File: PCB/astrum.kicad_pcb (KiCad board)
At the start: 4 copper layers, 45.5 x 69.8 mm, 60 parts, among them J1 USB_C_Receptacle_USB2.0_16P, J10 Conn_01x05_Pin, J11 Screw_Terminal_01x02, J2 Micro_SD_Card, J3 Screw_Terminal_01x02, J5 Conn_01x04_MountingPin, J6 Conn_01x04_MountingPin, J7 Conn_01x10_Pin, J8 Conn_01x10_Pin, J9 Conn_01x05_Pin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

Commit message: update production files
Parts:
- removed the G*** at (152.8, 124.0)
- removed the G*** at (146.8, 129.1)
- removed the G*** at (144.0, 129.1)
- removed the G*** at (153.0, 108.8)
- removed the G*** at (159.5, 129.1)
- removed the G*** at (142.8, 108.8)
- removed the G*** at (138.0, 124.0)
- removed the G*** at (131.2, 129.1)
- added C21: 100nF, A_HDJ_Library:C_0603_1608Metric, F.Cu at (162.3, 123.9)
- added C22: 100nF, A_HDJ_Library:C_0402_1005Metric, F.Cu at (149.4, 99.8)
- added G***: LOGO, LOGO, F.Cu at (146.3, 111.1)
- added G***: LOGO, LOGO, F.Cu at (156.5, 111.1)
- added G***: LOGO, LOGO, F.Cu at (134.8, 131.4)
- added G***: LOGO, LOGO, F.Cu at (147.5, 131.4)
- added G***: LOGO, LOGO, F.Cu at (163.0, 131.4)
- added G***: LOGO, LOGO, F.Cu at (156.3, 126.4)
- added G***: LOGO, LOGO, F.Cu at (150.3, 131.4)
- added G***: LOGO, LOGO, F.Cu at (141.5, 126.4)
- added R6: 4.7k, Resistor_SMD:R_0603_1608Metric, F.Cu at (152.9, 88.5)
- added R8: 10k, Resistor_SMD:R_0603_1608Metric, F.Cu at (135.3, 124.5)
- added SW1: TS-1088-AR02016, easyeda2kicad:SW-SMD_L3.9-W3.0-P4.45, F.Cu at (161.5, 119.8)
- added SW2: TS-1088-AR02016, easyeda2kicad:SW-SMD_L3.9-W3.0-P4.45, F.Cu at (136.1, 119.8)
- C18: value C_Polarized_Small -> 22uF
- C2: footprint A_HDJ_Library:C_0603_1608Metric -> lpddr4-testbed-footprints:C_0402_1005Metric
- moved C2 15.0 mm to (153.6, 92.1), turned to 0 degrees
- moved C12 4.24 mm to (136.3, 91.6)
- moved C18 4.24 mm to (148.9, 116.7)
- moved D3 4.24 mm to (137.1, 82.1)
- moved J3 4.24 mm to (138.8, 131.4)
- moved J5 4.24 mm to (132.7, 111.7)
- moved R3 4.24 mm to (145.5, 121.8)
- moved U4 4.24 mm to (158.4, 94.8)
- moved U9 4.24 mm to (156.0, 119.6)
- moved J2 4.24 mm to (154.7, 79.0)
- moved J8 4.24 mm to (131.5, 80.9)
- moved R2 4.24 mm to (133.4, 76.4)
- moved C1 4.24 mm to (142.5, 96.4)
- moved C10 4.24 mm to (137.7, 89.5)
- moved C11 4.24 mm to (158.4, 100.3)
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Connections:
- U1 pad 44: unconnected-(U1-BOOT0-Pad44) -> BOOT0
- U1 pad 7: unconnected-(U1-NRST-Pad7) -> NRST
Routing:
- net BOOT0: track 0.00 -> 38.7 mm, vias 0 -> 2
- net NRST: track 0.00 -> 37.5 mm, vias 0 -> 3
- net VDD: track 89.9 -> 92.9 mm, vias 16 -> 18
- net unconnected-(U1-BOOT0-Pad44): track 0.66 -> 0.00 mm, vias 1 -> 0
- net GND: vias 37 -> 35
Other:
- outline, holes or cut-outs redrawn

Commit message: make the board cheaper?
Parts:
- removed C14: 100nF, A_HDJ_Library:C_0603_1608Metric
- removed the G*** at (146.3, 111.1)
- removed the G*** at (156.5, 111.1)
- removed the G*** at (134.8, 131.4)
- removed the G*** at (147.5, 131.4)
- removed the G*** at (163.0, 131.4)
- removed the G*** at (156.3, 126.4)
- removed the G*** at (150.3, 131.4)
- removed the G*** at (141.5, 126.4)
- removed U5: ICM-20948, Sensor_Motion:InvenSense_QFN-24_3x3mm_P0.4mm
- removed Y1: 25 mHz, Crystal:Crystal_SMD_Abracon_ABM3-2Pin_5.0x3.2mm
- added G***: LOGO, LOGO, F.Cu at (135.7, 132.5)
- added G***: LOGO, LOGO, F.Cu at (157.2, 127.5)
- added G***: LOGO, LOGO, F.Cu at (151.2, 132.5)
- added G***: LOGO, LOGO, F.Cu at (157.5, 111.7)
- added G***: LOGO, LOGO, F.Cu at (142.5, 127.5)
- added G***: LOGO, LOGO, F.Cu at (147.3, 111.7)
- added G***: LOGO, LOGO, F.Cu at (164.0, 132.5)
- added G***: LOGO, LOGO, F.Cu at (148.5, 132.5)
- added R10: 10k, Resistor_SMD:R_0603_1608Metric, F.Cu at (137.3, 108.0)
- added R9: 10k, Resistor_SMD:R_0603_1608Metric, F.Cu at (140.3, 108.0)
- added U11: LD39015M18R, Package_TO_SOT_SMD:SOT-23-5, F.Cu at (137.9, 95.2)
- added Y2: 25mHz, Crystal:Crystal_SMD_3225-4Pin_3.2x2.5mm, F.Cu at (148.7, 104.7)
- C18: footprint Capacitor_SMD:CP_Elec_3x5.3 -> Capacitor_SMD:CP_Elec_4x5.4
- C20: value C_Polarized_Small -> 22uF; footprint Capacitor_SMD:CP_Elec_3x5.3 -> Capacitor_SMD:CP_Elec_4x5.4
- C7, C8: value 5.6pF -> 12pF
- U6: value MIC5317-1.8xM5 -> LSM6DSR; footprint Package_TO_SOT_SMD:SOT-23-5 -> LSM6DSR:LGA_M6DSR_STM
- moved U6 11.7 mm to (139.3, 105.5), turned to 180 degrees
- moved C16 3.52 mm to (139.0, 103.1), turned to 180 degrees
- moved C7 2.34 mm to (145.7, 104.8)
- moved C15 2.12 mm to (136.6, 105.6), turned to -90 degrees
- moved C20 1.85 mm to (149.8, 124.3)
- moved C21 1.47 mm to (163.2, 125.0)
- moved H1 1.47 mm to (130.0, 73.7)
- moved H2 1.47 mm to (169.5, 73.5)
- moved J7 1.47 mm to (167.0, 82.0)
- moved U1 1.47 mm to (149.4, 95.8)
- moved C11 1.47 mm to (159.4, 101.4)
- moved C13 1.47 mm to (140.7, 95.2)
- moved C2 1.47 mm to (154.6, 93.2)
- moved C3 1.47 mm to (145.8, 88.9)
- moved C5 1.47 mm to (145.8, 90.5)
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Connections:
- C15 pad 1: +1V8 -> VDD
- C16 pad 1: +1V8 -> VDD
- J7 pad 10: unconnected-(J7-Pin_10-Pad10) -> GND
- J7 pad 9: unconnected-(J7-Pin_9-Pad9) -> GND
- J8 pad 10: GPIO8 -> unconnected-(J8-Pin_10-Pad10)
- U6 pad 1: VDD -> unconnected-(U6-SDO/SA0-Pad1)
- U6 pad 2: GND -> unconnected-(U6-SDX-Pad2)
- U6 pad 3: VDD -> unconnected-(U6-SCX-Pad3)
- U6 pad 4: unconnected-(U6-NC-Pad4) -> GPIO8
- U6 pad 5: +1V8 -> VDD
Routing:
- net IMU_SDA: track 66.8 -> 83.2 mm, vias 4 -> 6
- net IMU_SCL: track 68.3 -> 83.9 mm, vias 4 -> 5
- net +1V8: track 97.9 -> 82.9 mm, vias 12 -> 9
- net IMU_INT: track 22.9 -> 36.2 mm, vias 2 -> 4
- net VDD: track 92.9 -> 102.0 mm, vias 18 -> 21
- net GPIO8: track 19.7 -> 12.9 mm, vias 1 -> 2
- net /SCL_1V8: track 10.5 -> 3.76 mm
- net /SDA_1V8: track 6.44 -> 1.58 mm
- net /INT_1V8: track 32.4 -> 29.6 mm, vias 2 -> 1
- net unconnected-(U5-SDO/AD0-Pad9): track 2.27 -> 0.00 mm, vias 1 -> 0
- net Net-(U5-REGOUT): track 2.22 -> 0.00 mm
- net Net-(U1-PH1): track 8.97 -> 6.77 mm
- net /FSYNC_1V8: track 2.72 -> 1.60 mm, vias 1 -> 0
- net GND: vias 35 -> 38
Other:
- board size 45.5 x 69.8 mm -> 45.5 x 69.7 mm

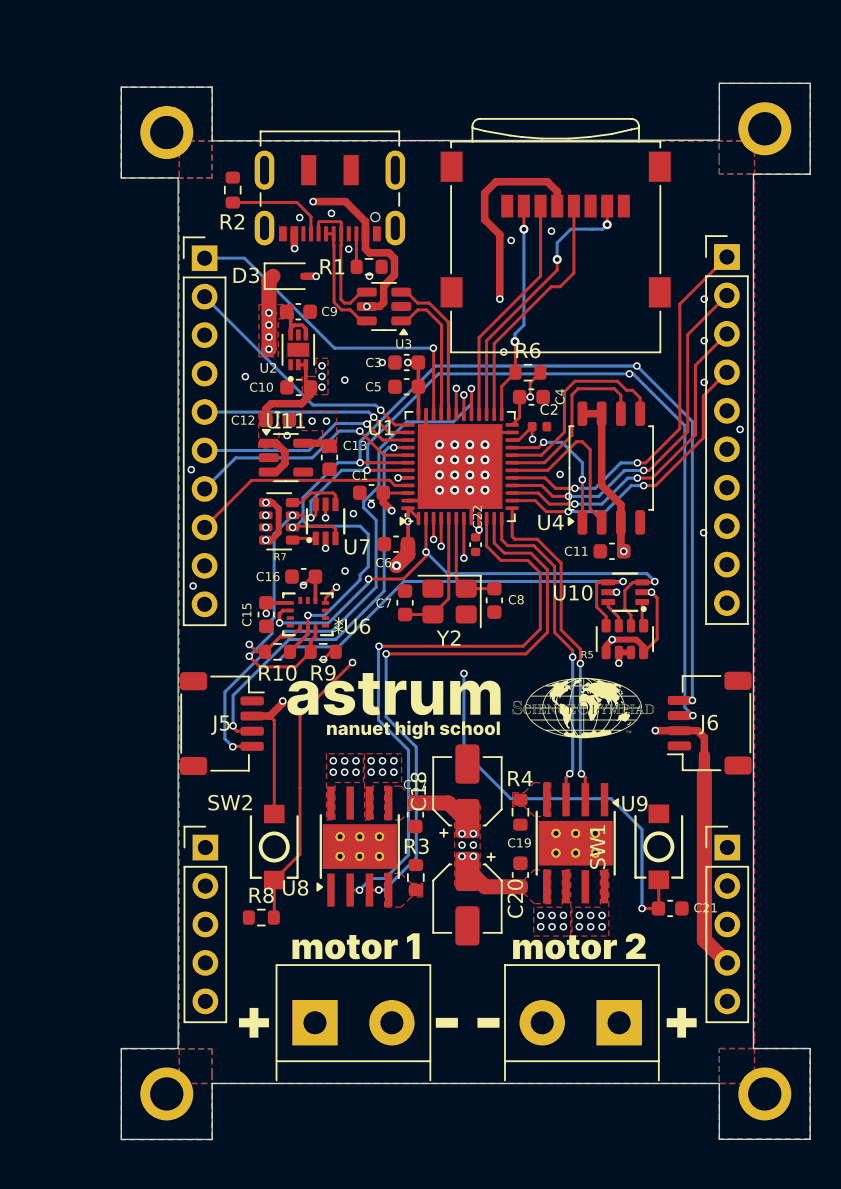
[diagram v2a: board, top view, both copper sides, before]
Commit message: fix oscillator
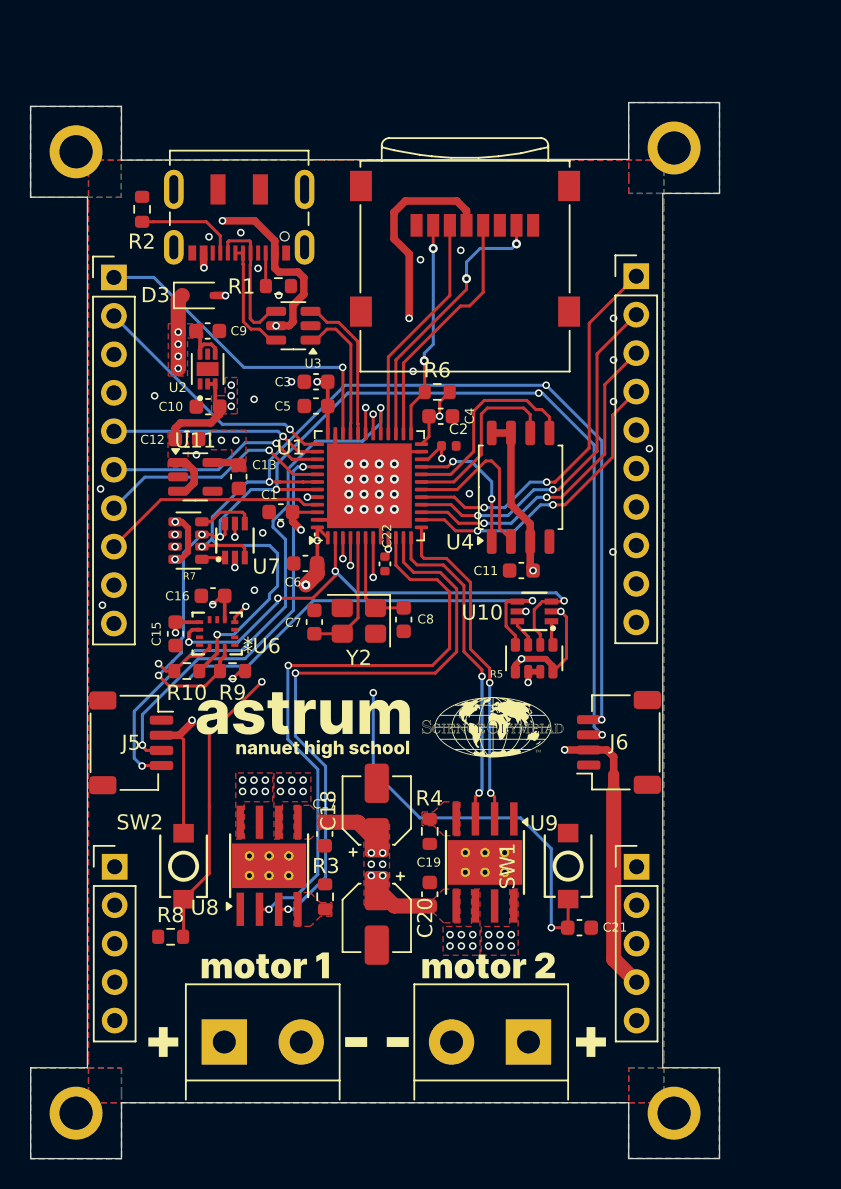
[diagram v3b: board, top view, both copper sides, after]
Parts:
- removed the G*** at (135.7, 132.5)
- removed the G*** at (157.2, 127.5)
- removed the G*** at (151.2, 132.5)
- removed the G*** at (157.5, 111.7)
- removed the G*** at (142.5, 127.5)
- removed the G*** at (147.3, 111.7)
- removed the G*** at (164.0, 132.5)
- removed the G*** at (148.5, 132.5)
- added G***: LOGO, LOGO, F.Cu at (141.3, 113.0)
- added G***: LOGO, LOGO, F.Cu at (151.5, 113.0)
- added G***: LOGO, LOGO, F.Cu at (129.8, 133.8)
- added G***: LOGO, LOGO, F.Cu at (136.5, 128.8)
- added G***: LOGO, LOGO, F.Cu at (145.2, 133.8)
- added G***: LOGO, LOGO, F.Cu at (142.5, 133.8)
- added G***: LOGO, LOGO, F.Cu at (151.2, 128.8)
- added G***: LOGO, LOGO, F.Cu at (158.0, 133.8)
- moved C13 6.12 mm to (134.7, 96.5)
- moved C15 6.12 mm to (130.6, 106.8)
- moved C2 6.12 mm to (148.6, 94.4)
- moved C5 6.12 mm to (139.8, 91.8)
- moved C8 6.12 mm to (145.6, 105.9)
- moved H3 6.12 mm to (163.5, 138.5)
- moved H4 6.12 mm to (124.0, 138.5)
- moved J11 6.12 mm to (153.9, 133.8)
- moved J3 6.12 mm to (133.8, 133.8)
- moved R5 6.12 mm to (154.3, 108.5)
- moved SW1 6.12 mm to (156.5, 122.2)
- moved U2 6.12 mm to (132.7, 89.4)
- moved U3 6.12 mm to (138.3, 86.5)
- moved C11 6.12 mm to (153.4, 102.7)
- moved C12 6.12 mm to (131.3, 94.0)
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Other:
- board size 45.5 x 69.7 mm -> 45.5 x 69.8 mm

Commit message: fix some dum vcap thingies
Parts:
- U2: footprint LDL212PV33R:SON50P200X200X80-7N -> LDL212PV33R:DFN_V33R_STM
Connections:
- net GPIO8 renamed IMU_INT1
- C1 pad 1: VDD -> Net-(C1-Pad1)
- C2 pad 1: VDD -> Net-(C1-Pad1)
- U1 pad 22: VDD -> Net-(C1-Pad1)
- U1 pad 46: VDD -> Net-(C1-Pad1)
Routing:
- net Net-(C1-Pad1): track 0.00 -> 18.7 mm, vias 0 -> 2
- net VDD: track 102.0 -> 96.3 mm, vias 21 -> 19

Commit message: update stuff again
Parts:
- removed the G*** at (141.3, 113.0)
- removed the G*** at (151.5, 113.0)
- removed the G*** at (129.8, 133.8)
- removed the G*** at (136.5, 128.8)
- removed the G*** at (145.2, 133.8)
- removed the G*** at (142.5, 133.8)
- removed the G*** at (151.2, 128.8)
- removed the G*** at (158.0, 133.8)
- added ?: , clipboard:975089c0-34e4-4fa3-ba18-6809d370517a, B.Cu at (162.0, 125.8)
- added ?: , clipboard:975089c0-34e4-4fa3-ba18-6809d370517a, B.Cu at (146.9, 125.8)
- added G***: LOGO, LOGO, F.Cu at (157.0, 108.8)
- added G***: LOGO, LOGO, B.Cu at (135.2, 129.6)
- added G***: LOGO, LOGO, B.Cu at (150.7, 129.6)
- added G***: LOGO, LOGO, B.Cu at (142.0, 124.5)
- added G***: LOGO, LOGO, B.Cu at (156.7, 124.5)
- added G***: LOGO, LOGO, B.Cu at (148.0, 129.6)
- added G***: LOGO, LOGO, B.Cu at (154.2, 93.5)
- added G***: LOGO, LOGO, B.Cu at (163.5, 129.6)
- added G***: LOGO, LOGO, F.Cu at (146.8, 108.8)
- added G***: LOGO, LOGO, F.Cu at (148.0, 129.6)
- added G***: LOGO, LOGO, F.Cu at (156.7, 124.5)
- added G*** (x2): LOGO, LOGO, F.Cu at (142.0, 124.5)
- added G***: LOGO, LOGO, F.Cu at (150.7, 129.6)
- added G***: LOGO, LOGO, F.Cu at (135.2, 129.6)
- added G***: LOGO, LOGO, F.Cu at (163.5, 129.6)
- C7, C8: value 12pF -> 18pF
- moved C13 6.94 mm to (140.2, 92.2)
- moved C2 6.94 mm to (154.1, 90.2)
- moved C5 6.94 mm to (145.3, 87.6)
- moved C8 6.94 mm to (151.1, 101.7)
- moved H3 6.94 mm to (169.0, 134.3)
- moved H4 6.94 mm to (129.5, 134.3)
- moved J11 6.94 mm to (159.4, 129.6)
- moved J3 6.94 mm to (139.3, 129.6)
- moved SW1 6.94 mm to (162.0, 117.9)
- moved U2 6.94 mm to (138.2, 85.1)
- moved U3 6.94 mm to (143.8, 82.3)
- moved C11 6.94 mm to (158.9, 98.4)
- moved C12 6.94 mm to (136.8, 89.7)
- moved C15 6.94 mm to (136.1, 102.6)
- moved C16 6.94 mm to (138.5, 100.1)
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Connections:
- net IMU_INT1 renamed GPIO8
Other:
- board size 45.5 x 69.8 mm -> 45.5 x 69.7 mm
